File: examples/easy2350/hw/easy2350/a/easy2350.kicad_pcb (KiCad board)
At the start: 4 copper layers, 21 x 51 mm, 58 parts, among them J1 USB-C, J2 GPIO left, J3 GPIO right, J4 SWD, SW1 BOOTSEL, SW2 RESET, U1 RP2350A, U2 USBLC6-2SC6, U3 AP7361C-33FGE, U4 SN74LV1T125DBVR, U5 W25Q128JVSIQ, Y1 12MHz

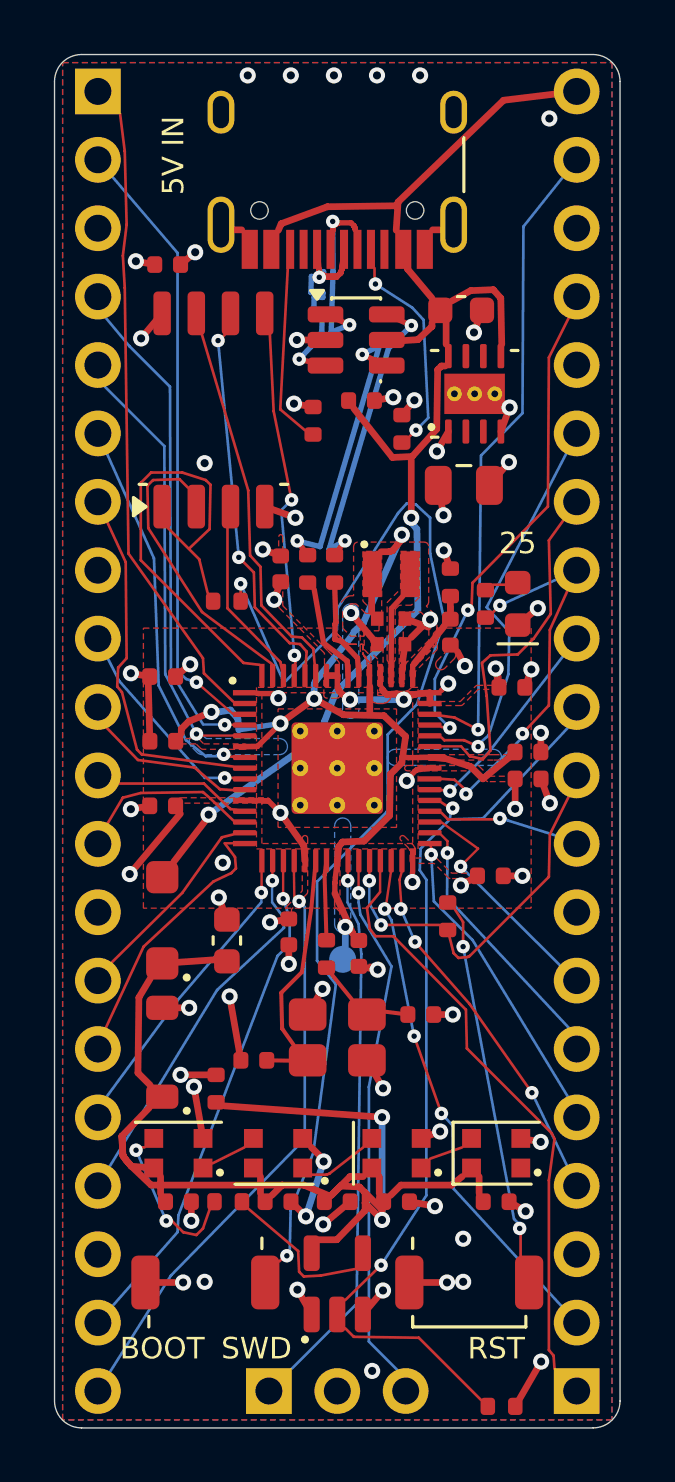
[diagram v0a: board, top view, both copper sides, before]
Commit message: easy2350: re-routed on ultraroute 4ed8d5d, reference zone islands joined; autoroute counts plane opens
DRC 0 errors, 0 unconnected, parity 0, no isolated copper or slivers;
pad_joints, silk, nets and placement checks pass.

autoroute.py now counts plane-net connections left open when it judges a
seed, apart from signal opens: stitching can't join every one (seed 0 left
C4/C17 grounded only to each other with no room for a via), so it tries the
next seed until one leaves none, and ranks them after signal opens.

Co-Authored-By: Claude Opus 5.5 <noreply@anthropic.com>
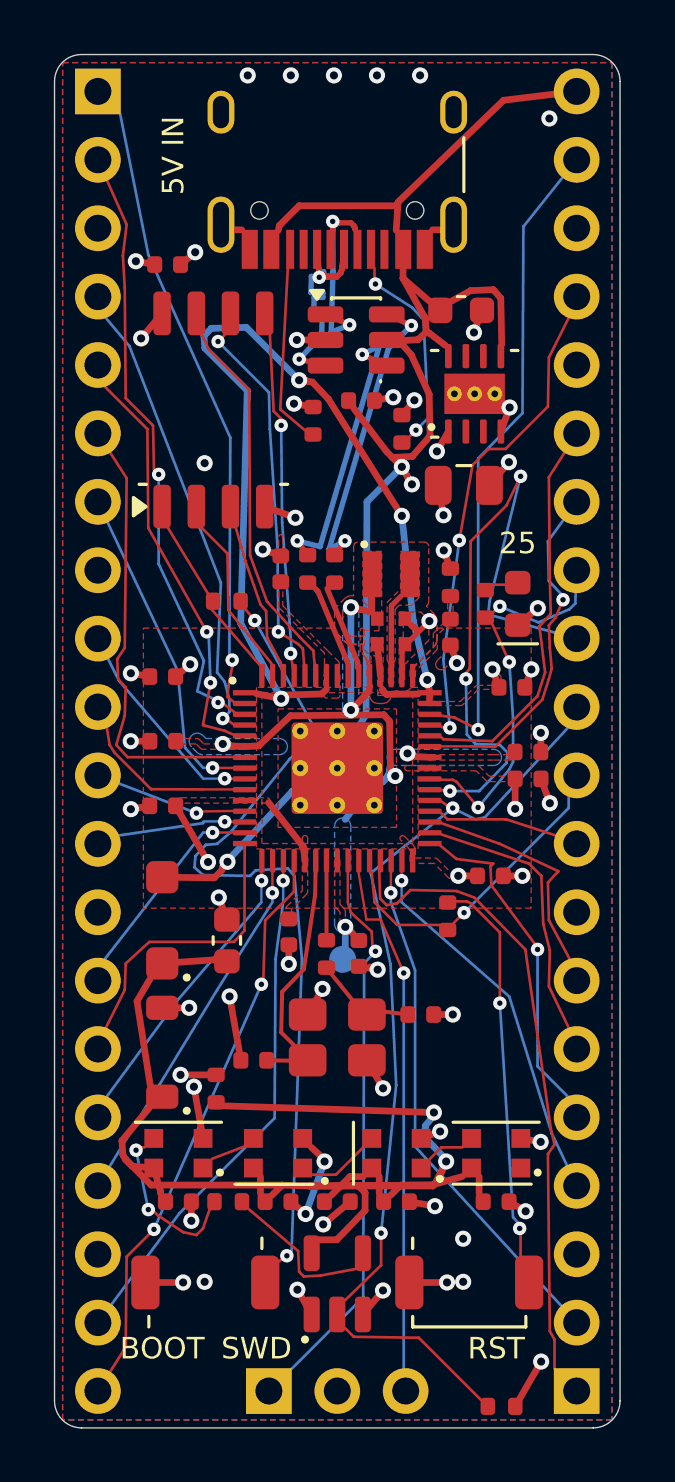
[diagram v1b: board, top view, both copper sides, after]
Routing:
- net +3V3: track 25.6 -> 50.6 mm, vias 21 -> 14
- net /GPIO24: track 7.66 -> 23.9 mm, vias 1 -> 3
- net +1V1: track 35.8 -> 20.8 mm, vias 5 -> 6
- net Net-(R7-Pad2): track 43.7 -> 30.8 mm
- net /QSPI_SS: track 17.3 -> 5.56 mm
- net VLED: track 42.2 -> 48.6 mm
- net VBUS: track 47.8 -> 53.9 mm, vias 2 -> 3
- net /QSPI_SD1: track 10.2 -> 6.00 mm
- net /RUN: track 13.1 -> 10.3 mm, vias 2 -> 1
- net /VREG_AVDD: track 2.65 -> 0.00 mm
- net /GPIO9: track 6.48 -> 4.30 mm, vias 0 -> 1
- net GND: track 48.7 -> 46.5 mm
- net /GPIO4: track 14.6 -> 16.7 mm, vias 1 -> 0
- net /GPIO11: track 9.22 -> 10.7 mm
- net /GPIO16: track 21.9 -> 23.3 mm
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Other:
- board text added: "not Pico pinout"
